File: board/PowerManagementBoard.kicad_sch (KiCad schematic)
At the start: 0 parts

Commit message: kitty!
5V and 3.3V
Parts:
- added C19, C20, C25, C26: C, symbol Device:C
- added U16: OKI-78SR-3.3_1.5-W36H-C, Converter_DCDC:Converter_DCDC_Murata_OKI-78SR_Horizontal, symbol Converter_DCDC:OKI-78SR-3.3_1.5-W36H-C
- added U17: OKI-78SR-5_1.5-W36H-C, Converter_DCDC:Converter_DCDC_Murata_OKI-78SR_Horizontal, symbol Converter_DCDC:OKI-78SR-5_1.5-W36H-C
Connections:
- new net +24V: C19.1, C25.1, U16.1 (IN), U17.1 (IN)
- new net +3V3: C20.1, U16.3 (OUT)
- new net +5V: C26.1, U17.3 (OUT)
- new net GND: C19.2, C20.2, C25.2, C26.2, U16.2 (GND), U17.2 (GND)

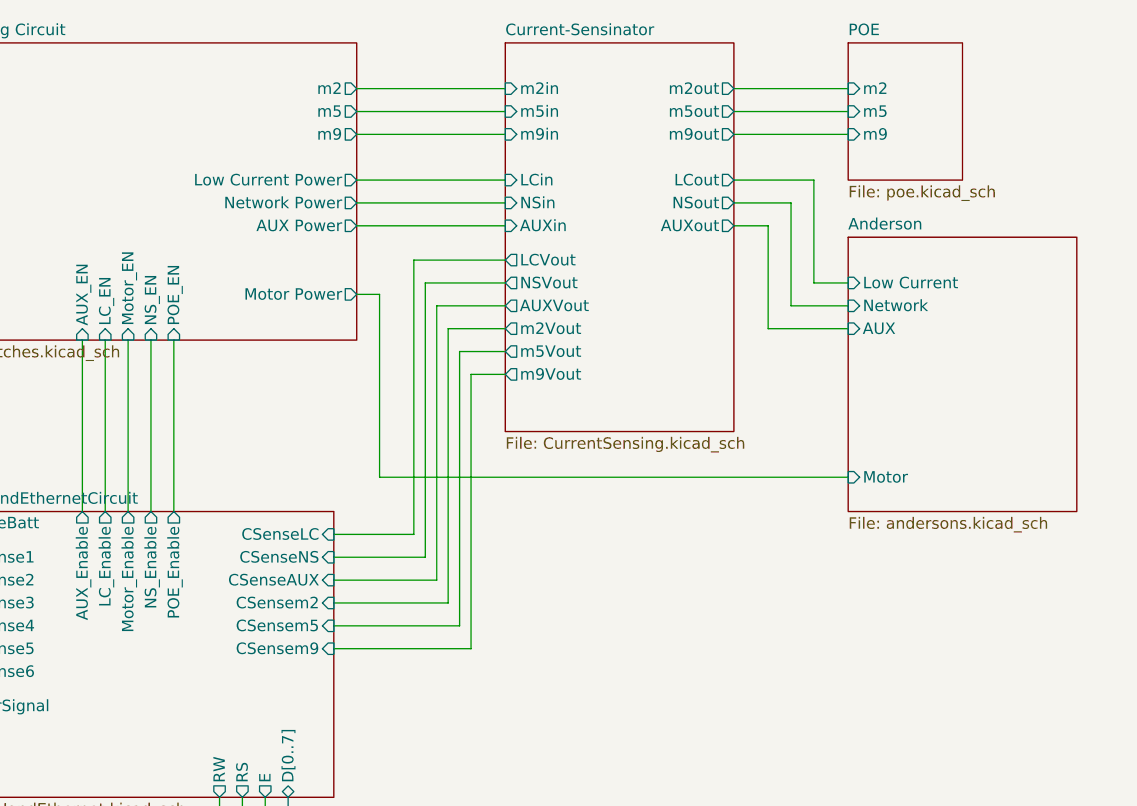
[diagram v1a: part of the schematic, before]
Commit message: include andersons for all LC and teensy enables for m2, m5, and m9
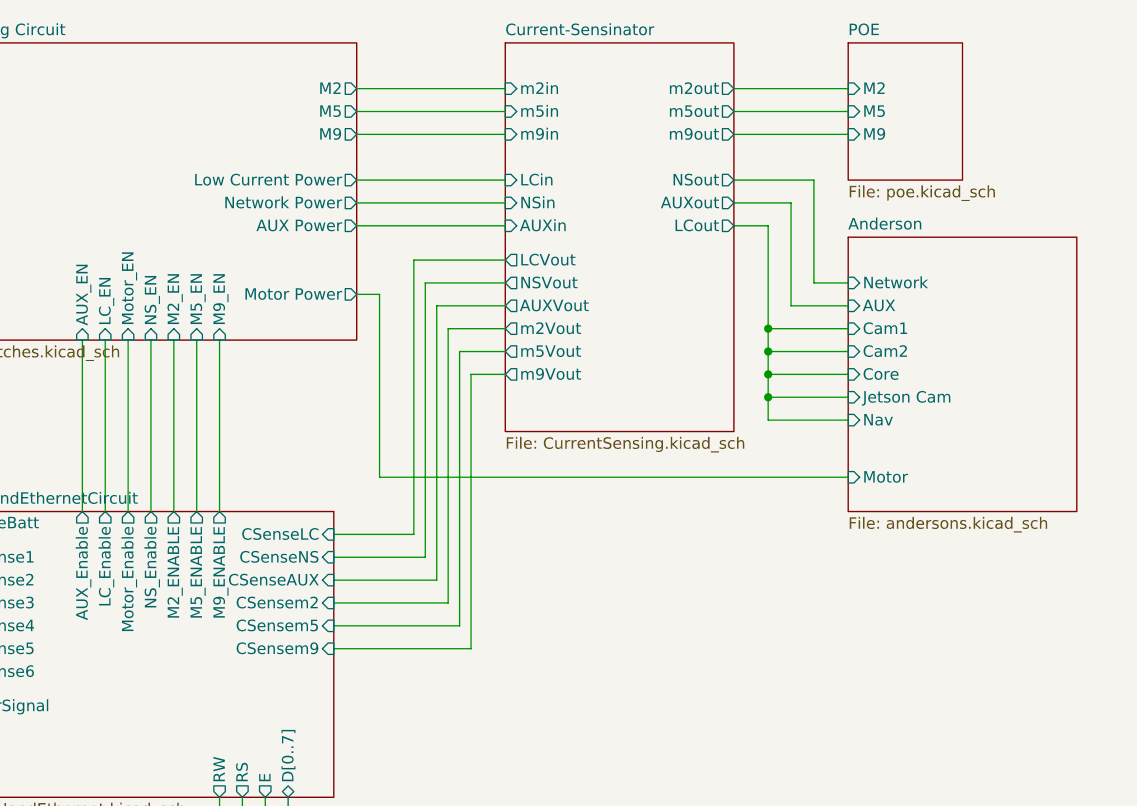
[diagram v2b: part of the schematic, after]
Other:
- sheet Anderson ports: added Cam1, Cam2, Core, Jetson Cam, Nav; removed Low Current
- sheet POE ports: added M2, M5, M9; removed m2, m5, m9
- sheet Switching Circuit ports: added M2, M2_EN, M5, M5_EN, M9, M9_EN; removed POE_EN, m2, m5, m9
- sheet TeensyandEthernetCircuit ports: added M2_ENABLE, M5_ENABLE, M9_ENABLE; removed POE_Enable
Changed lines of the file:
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@@
 	(paper "A4")
+	(junction
+		(at 168.91 57.15)
+		(diameter 0)
+		(color 0 0 0 0)
+	)
+	(junction
+		(at 168.91 59.69)
+		(diameter 0)
+		(color 0 0 0 0)
+	)
 	(junction
 		(at 113.03 182.88)
@@
 	)
 	(junction
+		(at 168.91 62.23)
+		(diameter 0)
+		(color 0 0 0 0)
+	)
+	(junction
 		(at 48.26 182.88)
+		(diameter 0)
+		(color 0 0 0 0)
+	)
+	(junction
+		(at 168.91 64.77)
 		(diameter 0)
 		(color 0 0 0 0)
@@
 	(wire
 		(pts
+			(xy 177.8 67.31) (xy 168.91 67.31)
+		)
+		(stroke
+			(width 0)
+			(type default)
+		)
+	)
+	(wire
+		(pts
 			(xy 177.8 54.61) (xy 171.45 54.61)
 		)
@@
 	(wire
 		(pts
+			(xy 105.41 58.42) (xy 105.41 77.47)
+		)
+		(stroke
+			(width 0)
+			(type default)
+		)
+	)
+	(wire
+		(pts
 			(xy 113.03 182.88) (xy 129.54 182.88)
 		)
@@
 	(wire
 		(pts
+			(xy 177.8 64.77) (xy 168.91 64.77)
+		)
+		(stroke
+			(width 0)
+			(type default)
+		)
+	)
+	(wire
+		(pts
 			(xy 132.08 85.09) (xy 132.08 54.61)
 		)
@@
 	(wire
 		(pts
+			(xy 168.91 62.23) (xy 168.91 59.69)
+		)
+		(stroke
+			(width 0)
+			(type default)
+		)
+	)
+	(wire
+		(pts
 			(xy 139.7 57.15) (xy 133.35 57.15)
 		)
@@
 	(wire
 		(pts
+			(xy 168.91 59.69) (xy 168.91 57.15)
+		)
+		(stroke
+			(width 0)
+			(type default)
+		)
+	)
+	(wire
+		(pts
 			(xy 139.7 62.23) (xy 135.89 62.23)
 		)
@@
 	(wire
 		(pts
+			(xy 168.91 64.77) (xy 168.91 62.23)
+		)
+		(stroke
+			(width 0)
+			(type default)
+		)
+	)
+	(wire
+		(pts
 			(xy 165.1 40.64) (xy 173.99 40.64)
 		)
@@
 	(wire
 		(pts
+			(xy 168.91 67.31) (xy 168.91 64.77)
+		)
+		(stroke
+			(width 0)
+			(type default)
+		)
+	)
+	(wire
+		(pts
 			(xy 64.77 162.56) (xy 64.77 170.18)
 		)
@@
 	(wire
 		(pts
+			(xy 102.87 58.42) (xy 102.87 77.47)
+		)
+		(stroke
+			(width 0)
+			(type default)
+		)
+	)
+	(wire
+		(pts
 			(xy 123.19 53.34) (xy 125.73 53.34)
 		)
@@
 	(wire
 		(pts
+			(xy 177.8 62.23) (xy 168.91 62.23)
+		)
+		(stroke
+			(width 0)
+			(type default)
+		)
+	)
+	(wire
+		(pts
 			(xy 165.1 35.56) (xy 177.8 35.56)
 		)
@@
 	(wire
 		(pts
-			(xy 102.87 58.42) (xy 102.87 77.47)
+			(xy 177.8 59.69) (xy 168.91 59.69)
+		)
+		(stroke
+			(width 0)
+			(type default)
+		)
+	)
+	(wire
+		(pts
+			(xy 107.95 58.42) (xy 107.95 77.47)
 		)
 		(stroke
@@
 			)
 		)
-		(pin "POE_Enable" output
-			(at 102.87 77.47 90)
-			(effects
-				(font
-					(size 1.27 1.27)
-				)
-				(justify right)
-			)
-		)
 		(pin "CSenseBatt" input
 			(at 76.2 78.74 180)
@@
 		(pin "CSenseNS" input
 			(at 120.65 82.55 0)
+			(effects
+				(font
+					(size 1.27 1.27)
+				)
+				(justify right)
+			)
+		)
+		(pin "M2_ENABLE" output
+			(at 102.87 77.47 90)
+			(effects
+				(font
+					(size 1.27 1.27)
+				)
+				(justify right)
+			)
+		)
+		(pin "M5_ENABLE" output
+			(at 105.41 77.47 90)
+			(effects
+				(font
+					(size 1.27 1.27)
+				)
+				(justify right)
+			)
+		)
+		(pin "M9_ENABLE" output
+			(at 107.95 77.47 90)
 			(effects
 				(font
@@
 		)
 		(pin "AUXout" output
-			(at 165.1 45.72 0)
+			(at 165.1 43.18 0)
 			(effects
 				(font
@@
 		)
 		(pin "LCout" output
-			(at 165.1 40.64 0)
+			(at 165.1 45.72 0)
 			(effects
 				(font
@@
 		)
 		(pin "NSout" output
-			(at 165.1 43.18 0)
+			(at 165.1 40.64 0)
 			(effects
 				(font
@@
 		)
 		(pin "AUX" input
-			(at 177.8 57.15 180)
-			(effects
-				(font
-					(size 1.27 1.27)
-				)
-				(justify left)
-			)
-		)
-		(pin "Low Current" input
-			(at 177.8 52.07 180)
+			(at 177.8 54.61 180)
 			(effects
 				(font
@@
 		)
 		(pin "Network" input
-			(at 177.8 54.61 180)
+			(at 177.8 52.07 180)
+			(effects
+				(font
+					(size 1.27 1.27)
+				)
+				(justify left)
+			)
+		)
+		(pin "Cam1" input
+			(at 177.8 57.15 180)
+			(effects
+				(font
+					(size 1.27 1.27)
+				)
+				(justify left)
+			)
+		)
+		(pin "Cam2" input
+			(at 177.8 59.69 180)
+			(effects
+				(font
+					(size 1.27 1.27)
+				)
+				(justify left)
+			)
+		)
+		(pin "Core" input
+			(at 177.8 62.23 180)
+			(effects
+				(font
+					(size 1.27 1.27)
+				)
+				(justify left)
+			)
+		)
+		(pin "Jetson Cam" input
+			(at 177.8 64.77 180)
+			(effects
+				(font
+					(size 1.27 1.27)
+				)
+				(justify left)
+			)
+		)
+		(pin "Nav" input
+			(at 177.8 67.31 180)
 			(effects
 				(font
@@
 			)
 		)
-		(pin "m2" input
+		(pin "M2" input
 			(at 177.8 30.48 180)
 			(effects
@@
 			)
 		)
-		(pin "m5" input
+		(pin "M5" input
 			(at 177.8 33.02 180)
 			(effects
@@
 			)
 		)
-		(pin "m9" input
+		(pin "M9" input
 			(at 177.8 35.56 180)
 			(effects
@@
 			)
 		)
-		(pin "POE_EN" input
-			(at 102.87 58.42 270)
-			(effects
-				(font
-					(size 1.27 1.27)
-				)
-				(justify left)
-			)
-		)
 		(pin "Vin" input
 			(at 76.2 48.26 180)
@@
 			)
 		)
-		(pin "m2" output
-			(at 123.19 30.48 0)
-			(effects
-				(font
-					(size 1.27 1.27)
-				)
-				(justify right)
-			)
-		)
-		(pin "m5" output
-			(at 123.19 33.02 0)
-			(effects
-				(font
-					(size 1.27 1.27)
-				)
-				(justify right)
-			)
-		)
-		(pin "m9" output
-			(at 123.19 35.56 0)
-			(effects
-				(font
-					(size 1.27 1.27)
-				)
-				(justify right)
-			)
-		)
 		(pin "Network Power" output
 			(at 123.19 43.18 0)
@@
 			)
 		)
+		(pin "M2" output
+			(at 123.19 30.48 0)
+			(effects
+				(font
+					(size 1.27 1.27)
+				)
+				(justify right)
+			)
+		)
+		(pin "M2_EN" input
+			(at 102.87 58.42 270)
+			(effects
+				(font
+					(size 1.27 1.27)
+				)
+				(justify left)
+			)
+		)
+		(pin "M5" output
+			(at 123.19 33.02 0)
+			(effects
+				(font
+					(size 1.27 1.27)
+				)
+				(justify right)
+			)
+		)
+		(pin "M5_EN" input
+			(at 105.41 58.42 270)
+			(effects
+				(font
+					(size 1.27 1.27)
+				)
+				(justify left)
+			)
+		)
+		(pin "M9" output
+			(at 123.19 35.56 0)
+			(effects
+				(font
+					(size 1.27 1.27)
+				)
+				(justify right)
+			)
+		)
+		(pin "M9_EN" input
+			(at 107.95 58.42 270)
+			(effects
+				(font
+					(size 1.27 1.27)
+				)
+				(justify left)
+			)
+		)

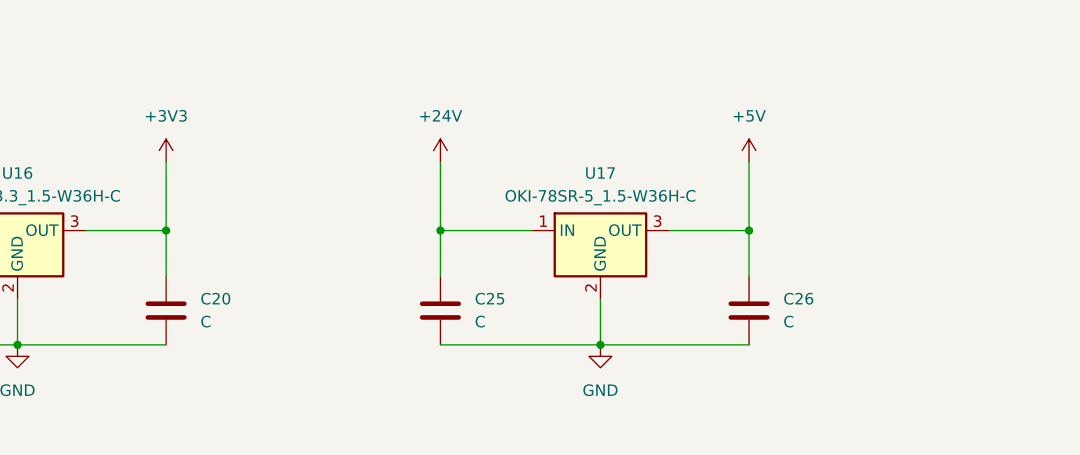
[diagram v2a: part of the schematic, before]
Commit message: added power leds
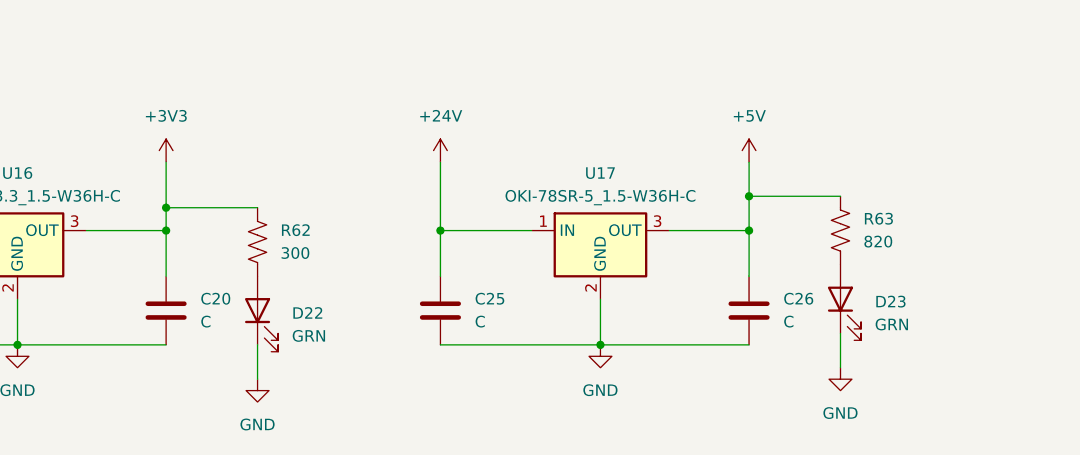
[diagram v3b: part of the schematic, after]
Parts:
- added D22, D23: GRN, symbol Device:LED
- added R62: 300, symbol Device:R_US
- added R63: 820, symbol Device:R_US
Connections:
- net +3V3: now also R62.1
- net +5V: now also R63.1
- net GND: now also D22.1 (K), D23.1 (K)
- new net: D22.2 (A), R62.2
- new net: D23.2 (A), R63.2

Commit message: More footprints added
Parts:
- C19, C20, C25, C26: footprint (none) -> Capacitor_SMD:C_0603_1608Metric
- D22, D23: footprint (none) -> Diode_SMD:D_0603_1608Metric
- R62, R63: footprint (none) -> Resistor_SMD:R_0603_1608Metric
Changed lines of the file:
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@@
 			)
 		)
-		(property "Footprint" ""
+		(property "Footprint" "Resistor_SMD:R_0603_1608Metric"
 			(at 75.946 171.704 90)
 			(effects
@@
 			)
 		)
-		(property "Footprint" ""
+		(property "Footprint" "Capacitor_SMD:C_0603_1608Metric"
 			(at 96.2152 182.88 0)
 			(effects
@@
 			)
 		)
-		(property "Footprint" ""
+		(property "Footprint" "Resistor_SMD:R_0603_1608Metric"
 			(at 140.716 170.434 90)
 			(effects
@@
 			)
 		)
-		(property "Footprint" ""
+		(property "Footprint" "Capacitor_SMD:C_0603_1608Metric"
 			(at 130.5052 182.88 0)
 			(effects
@@
 			)
 		)
-		(property "Footprint" ""
+		(property "Footprint" "Diode_SMD:D_0603_1608Metric"
 			(at 139.7 177.8 0)
 			(effects
@@
 			)
 		)
-		(property "Footprint" ""
+		(property "Footprint" "Capacitor_SMD:C_0603_1608Metric"
 			(at 31.4452 182.88 0)
 			(effects
@@
 			)
 		)
-		(property "Footprint" ""
+		(property "Footprint" "Diode_SMD:D_0603_1608Metric"
 			(at 74.93 179.07 0)
 			(effects
@@
 			)
 		)
-		(property "Footprint" ""
+		(property "Footprint" "Capacitor_SMD:C_0603_1608Metric"
 			(at 65.7352 182.88 0)
 			(effects

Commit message: Changed footprints to handsolder version
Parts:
- C19, C20, C25, C26: footprint Capacitor_SMD:C_0603_1608Metric -> Capacitor_SMD:C_0603_1608Metric_Pad1.08x0.95mm_HandSolder
- D22, D23: footprint Diode_SMD:D_0603_1608Metric -> LED_SMD:LED_0603_1608Metric_Pad1.05x0.95mm_HandSolder
- R62, R63: footprint Resistor_SMD:R_0603_1608Metric -> Resistor_SMD:R_0603_1608Metric_Pad0.98x0.95mm_HandSolder
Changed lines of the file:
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@@
 			)
 		)
-		(property "Footprint" "Resistor_SMD:R_0603_1608Metric"
+		(property "Footprint" "Resistor_SMD:R_0603_1608Metric_Pad0.98x0.95mm_HandSolder"
 			(at 75.946 171.704 90)
 			(effects
@@
 			)
 		)
-		(property "Footprint" "Capacitor_SMD:C_0603_1608Metric"
+		(property "Footprint" "Capacitor_SMD:C_0603_1608Metric_Pad1.08x0.95mm_HandSolder"
 			(at 96.2152 182.88 0)
 			(effects
@@
 			)
 		)
-		(property "Footprint" "Resistor_SMD:R_0603_1608Metric"
+		(property "Footprint" "Resistor_SMD:R_0603_1608Metric_Pad0.98x0.95mm_HandSolder"
 			(at 140.716 170.434 90)
 			(effects
@@
 			)
 		)
-		(property "Footprint" "Capacitor_SMD:C_0603_1608Metric"
+		(property "Footprint" "Capacitor_SMD:C_0603_1608Metric_Pad1.08x0.95mm_HandSolder"
 			(at 130.5052 182.88 0)
 			(effects
@@
 			)
 		)
-		(property "Footprint" "Diode_SMD:D_0603_1608Metric"
+		(property "Footprint" "LED_SMD:LED_0603_1608Metric_Pad1.05x0.95mm_HandSolder"
 			(at 139.7 177.8 0)
 			(effects
@@
 			)
 		)
-		(property "Footprint" "Capacitor_SMD:C_0603_1608Metric"
+		(property "Footprint" "Capacitor_SMD:C_0603_1608Metric_Pad1.08x0.95mm_HandSolder"
 			(at 31.4452 182.88 0)
 			(effects
@@
 			)
 		)
-		(property "Footprint" "Diode_SMD:D_0603_1608Metric"
+		(property "Footprint" "LED_SMD:LED_0603_1608Metric_Pad1.05x0.95mm_HandSolder"
 			(at 74.93 179.07 0)
 			(effects
@@
 			)
 		)
-		(property "Footprint" "Capacitor_SMD:C_0603_1608Metric"
+		(property "Footprint" "Capacitor_SMD:C_0603_1608Metric_Pad1.08x0.95mm_HandSolder"
 			(at 65.7352 182.88 0)
 			(effects

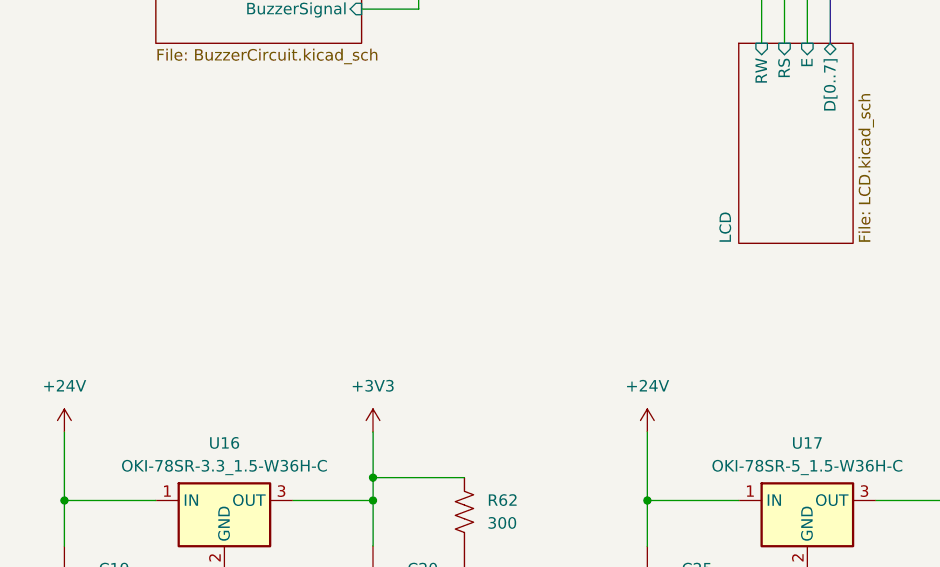
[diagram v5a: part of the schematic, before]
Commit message: Added mounting holes
added mounting holes and assigned them a footprint
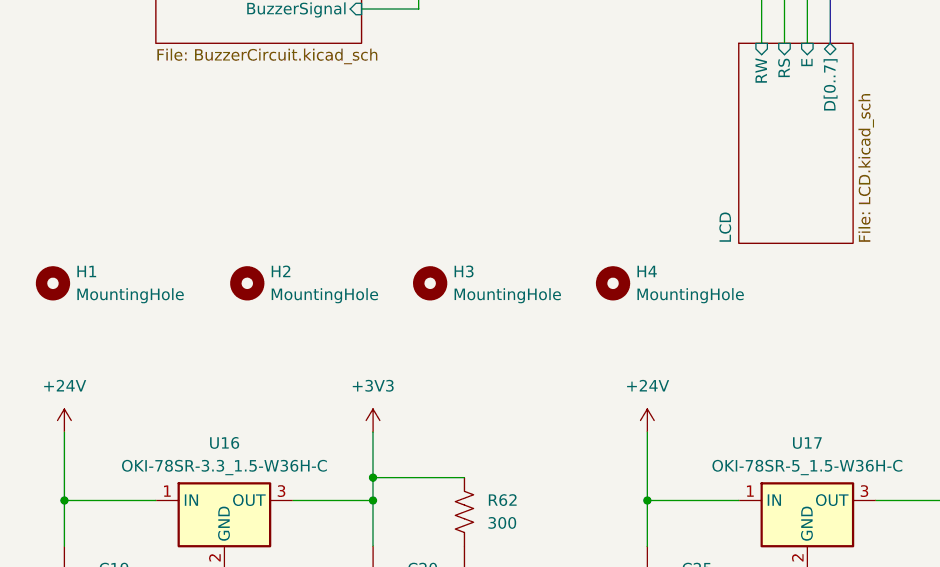
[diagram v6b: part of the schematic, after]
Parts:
- added H1, H2, H3, H4: MountingHole, MRDT_Drill_Holes:4_40_Hole_Corner, symbol Mechanical:MountingHole

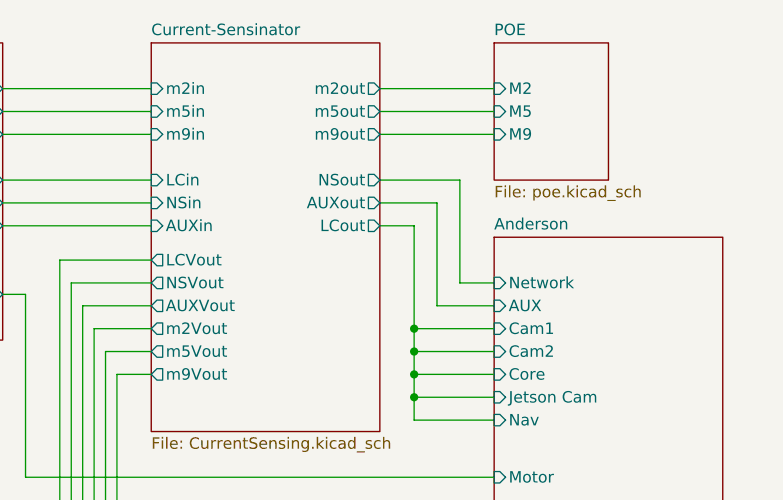
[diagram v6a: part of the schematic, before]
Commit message: designated an area for each circuit on pcb
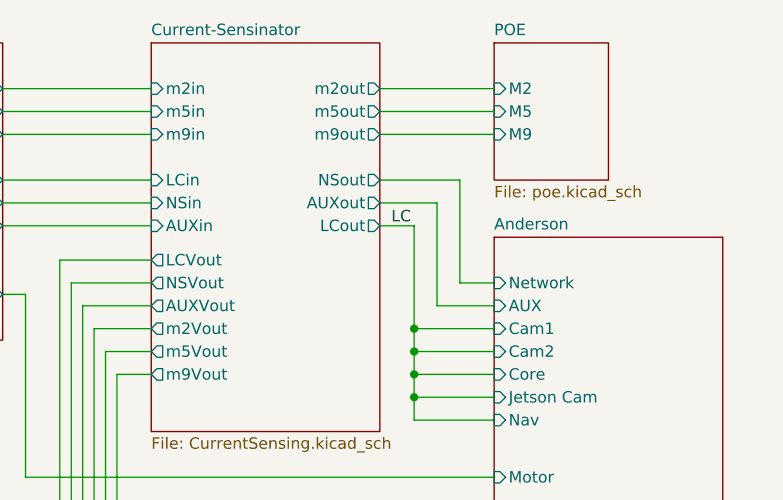
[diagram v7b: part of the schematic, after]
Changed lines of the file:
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@@
+		)
+	)
+	(label "LC"
+		(at 166.37 45.72 0)
+		(effects
+			(font
+				(size 1.27 1.27)
+			)
+			(justify left bottom)
 		)
 	)

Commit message: experimented with layout
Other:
- sheet Current-Sensinator ports: added none; removed m5out
- sheet POE ports: added none; removed M5
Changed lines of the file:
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@@
 	(wire
 		(pts
-			(xy 165.1 33.02) (xy 177.8 33.02)
-		)
-		(stroke
-			(width 0)
-			(type default)
-		)
-	)
-	(wire
-		(pts
 			(xy 64.77 170.18) (xy 64.77 175.26)
 		)
@@
 	(wire
 		(pts
-			(xy 165.1 35.56) (xy 177.8 35.56)
+			(xy 165.1 33.02) (xy 177.8 33.02)
 		)
 		(stroke
@@
 			)
 		)
-		(pin "m5out" output
-			(at 165.1 33.02 0)
-			(effects
-				(font
-					(size 1.27 1.27)
-				)
-				(justify right)
-			)
-		)
 		(pin "m5Vout" output
 			(at 139.7 59.69 180)
@@
 		)
 		(pin "m9out" output
-			(at 165.1 35.56 0)
+			(at 165.1 33.02 0)
 			(effects
 				(font
@@
 			)
 		)
-		(pin "M5" input
-			(at 177.8 33.02 180)
-			(effects
-				(font
-					(size 1.27 1.27)
-				)
-				(justify left)
-			)
-		)
 		(pin "M9" input
-			(at 177.8 35.56 180)
+			(at 177.8 33.02 180)
 			(effects
 				(font
